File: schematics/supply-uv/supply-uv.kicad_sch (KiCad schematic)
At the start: 12 parts, among them J1 VSYS connector to Board#2, J2 power +5V connector to board#2, J3 +5V_PWR (with fuse), J4 PWR_OUT (with fuse), U1 ISO1540

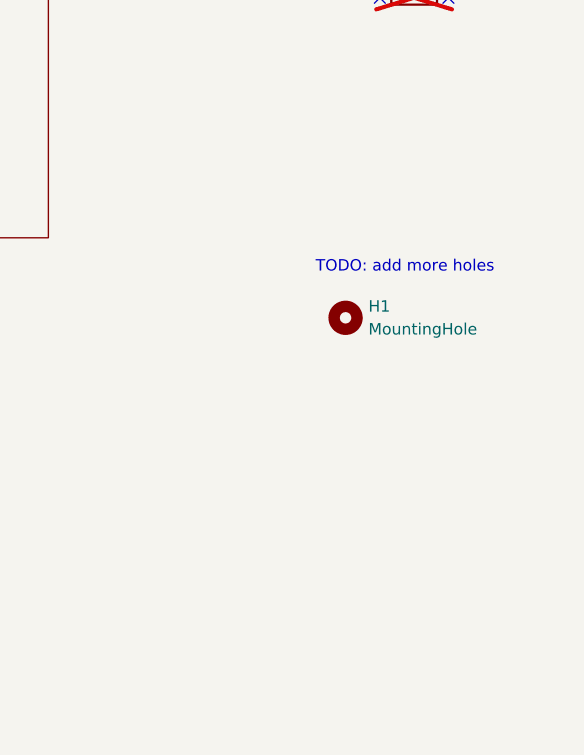
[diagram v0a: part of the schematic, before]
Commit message: first board routed
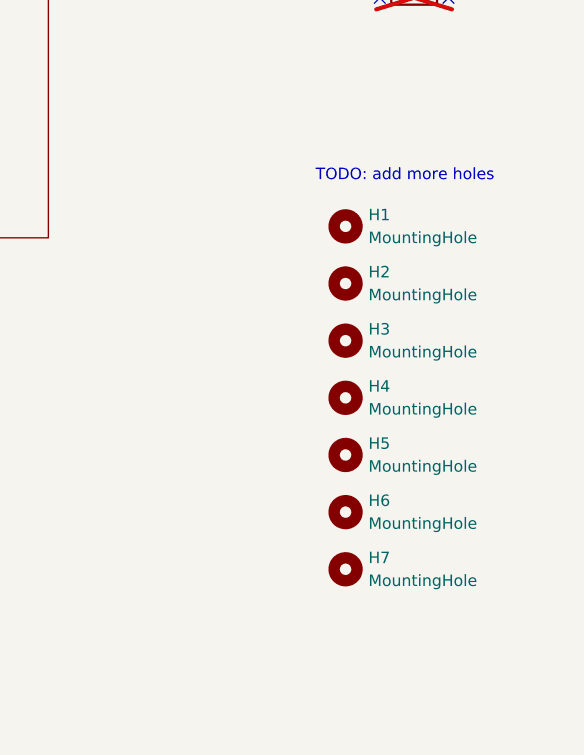
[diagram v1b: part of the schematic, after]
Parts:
- added H2, H3, H4, H5, H6, H7: MountingHole, MountingHole:MountingHole_2.2mm_M2, symbol Mechanical:MountingHole
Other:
- moved on the sheet: H1

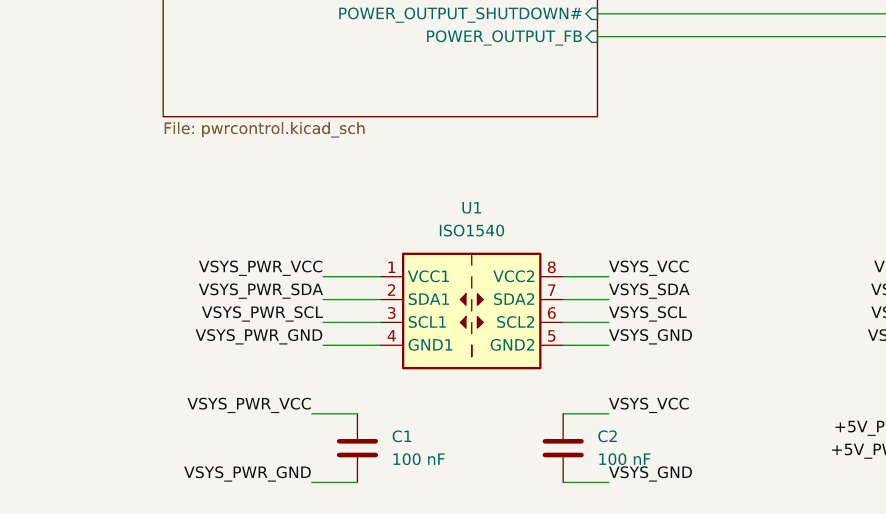
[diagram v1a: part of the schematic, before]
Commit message: power board works (except power output driver, not tested yet), I ready to solder control board
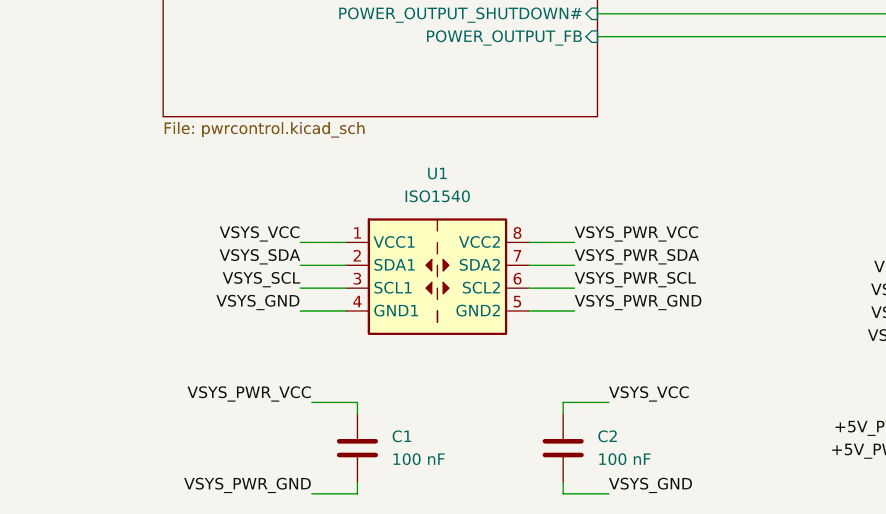
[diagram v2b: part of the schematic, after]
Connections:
- net VSYS_GND: now also U1.4 (GND1); no longer U1.5 (GND2)
- net VSYS_PWR_GND: now also U1.5 (GND2); no longer U1.4 (GND1)
- net VSYS_PWR_SCL: now also U1.6 (SCL2); no longer U1.3 (SCL1)
- net VSYS_PWR_SDA: now also U1.7 (SDA2); no longer U1.2 (SDA1)
- net VSYS_PWR_VCC: now also U1.8 (VCC2); no longer U1.1 (VCC1)
- net VSYS_SCL: now also U1.3 (SCL1); no longer U1.6 (SCL2)
- net VSYS_SDA: now also U1.2 (SDA1); no longer U1.7 (SDA2)
- net VSYS_VCC: now also U1.1 (VCC1); no longer U1.8 (VCC2)
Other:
- moved on the sheet: U1
